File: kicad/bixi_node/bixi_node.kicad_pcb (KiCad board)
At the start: 2 copper layers, 47 x 24.5 mm, 8 parts, among them J1 RJ45, J2 Screw_Terminal_1x01, J3 Screw_Terminal_1x01, P1 CONN_01X03, U1 SP3485CN

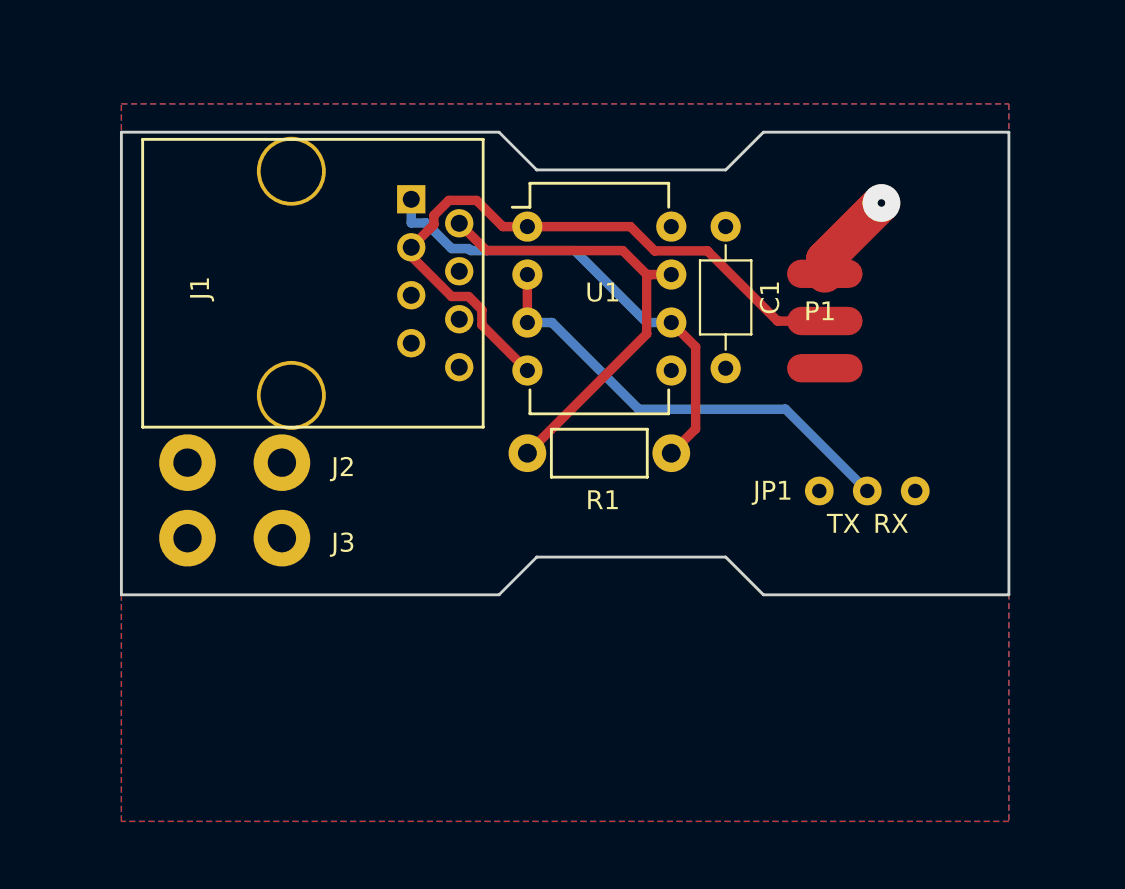
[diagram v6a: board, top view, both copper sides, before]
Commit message: v3 boards almost complete. added xcvr breakout, passthrough boards
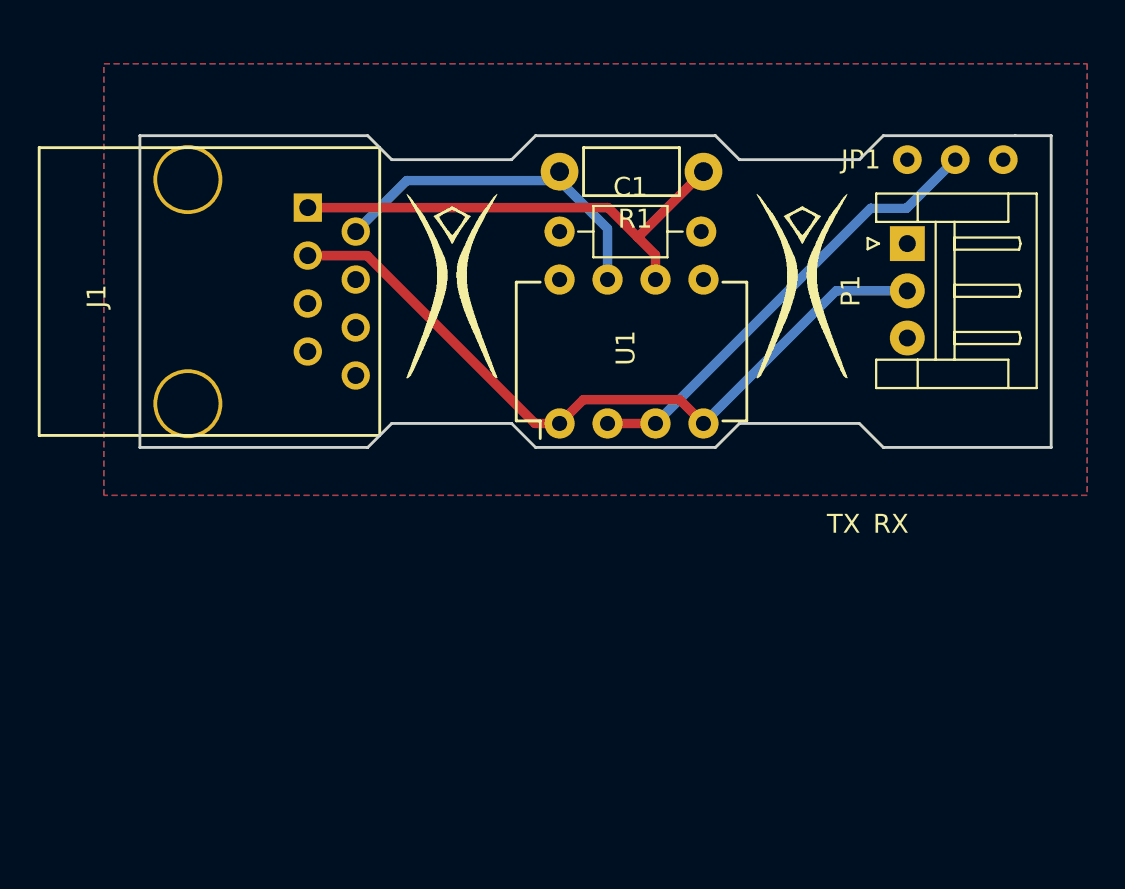
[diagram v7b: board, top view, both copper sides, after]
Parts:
- removed J2, J3: Screw_Terminal_1x01, custom:A116169CT_SPADE_CONNECTOR
- added burner-logo: , logos:burner-logo-fs, F.Cu at (106.9, 85.3)
- added burner-logo: , logos:burner-logo-fs, F.Cu at (125.5, 85.3)
- P1: footprint custom:PAD_3X_OVAL_WS2812B -> Connectors_JST:JST_EH_S03B-EH_03x2.50mm_Angled
- moved JP1 18.2 mm to (137.2, 84.5)
- moved R1 15.0 mm to (116.2, 85.1)
- moved U1 10.6 mm to (116.2, 98.4), turned to 90 degrees
- moved C1 8.80 mm to (116.2, 88.3), turned to 0 degrees
- moved P1 6.18 mm to (134.6, 88.9), turned to 270 degrees
- moved J1 5.50 mm to (96.5, 91.4)
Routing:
- net /DATA_DIFF_B: track 24.4 -> 18.7 mm
- net GND: track 4.99 -> 0.00 mm, vias 1 -> 0
- net /DATA: track 35.5 -> 39.4 mm
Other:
- board size 47 x 24.5 mm -> 48.3 x 16.5 mm
- net class Default: trace_width 2 -> 0.5; via_dia 2 -> 0.5

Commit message: v3 pcb's plotted, ready for fab
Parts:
- P1: footprint Connectors_JST:JST_EH_S03B-EH_03x2.50mm_Angled -> custom:PAD_3X_OVAL_WS2812B
- moved JP1 13.4 mm to (137.8, 97.8)
- moved P1 4.58 mm to (138.4, 91.4), turned to 180 degrees
- renumbered burner-logo to burner-logo1, burner-logo to burner-logo2
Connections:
- J1 pad 3: /DATA -> Net-(J1-Pad3)
- J1 pad 5: VCC -> Net-(J1-Pad5)
- J1 pad 6: VCC -> Net-(J1-Pad6)
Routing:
- net /DATA: track 39.4 -> 26.7 mm
- net GND: track 0.00 -> 5.35 mm, vias 0 -> 1
- net /MODE: track 24.2 -> 20.9 mm
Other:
- net class Default: trace_width 0.5 -> 2; via_dia 0.5 -> 2; via_drill 0.4 -> 1
